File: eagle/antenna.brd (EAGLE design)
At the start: 127 x 76.2 mm, 21 parts

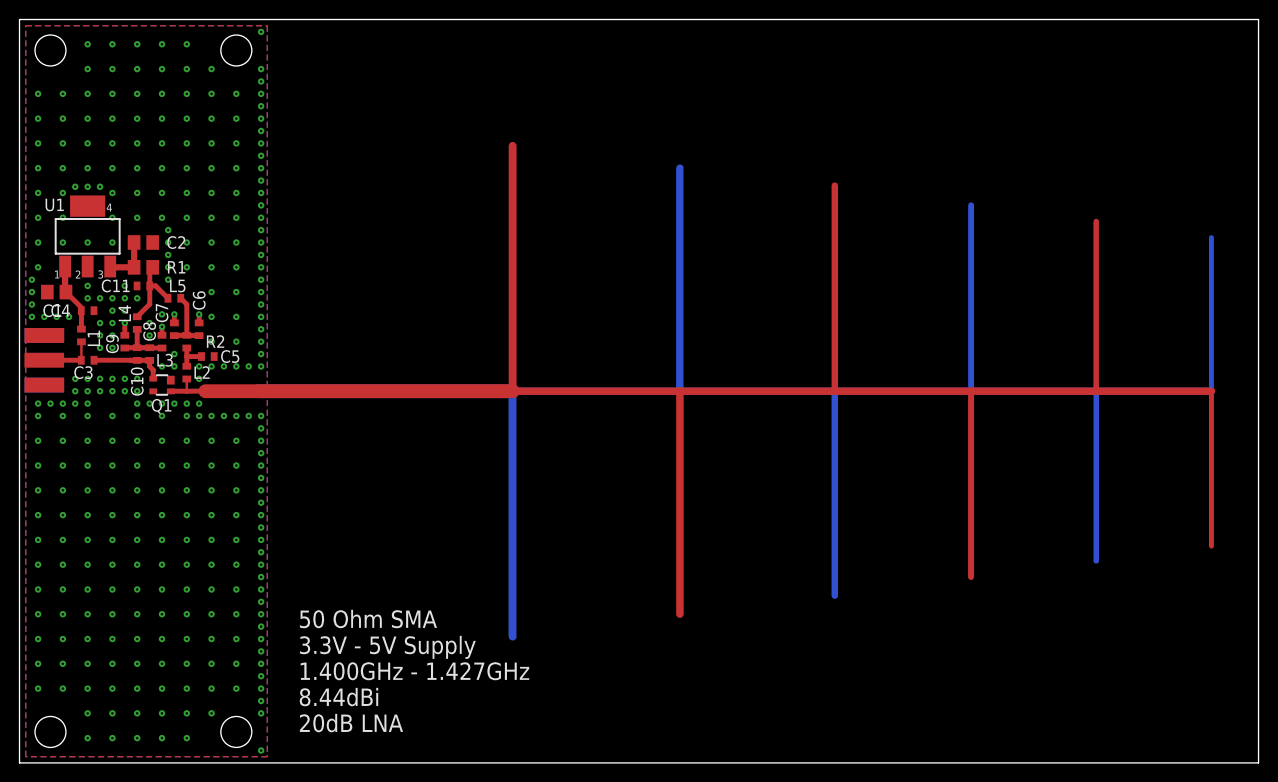
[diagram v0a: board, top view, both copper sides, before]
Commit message: cleaner antenna layout
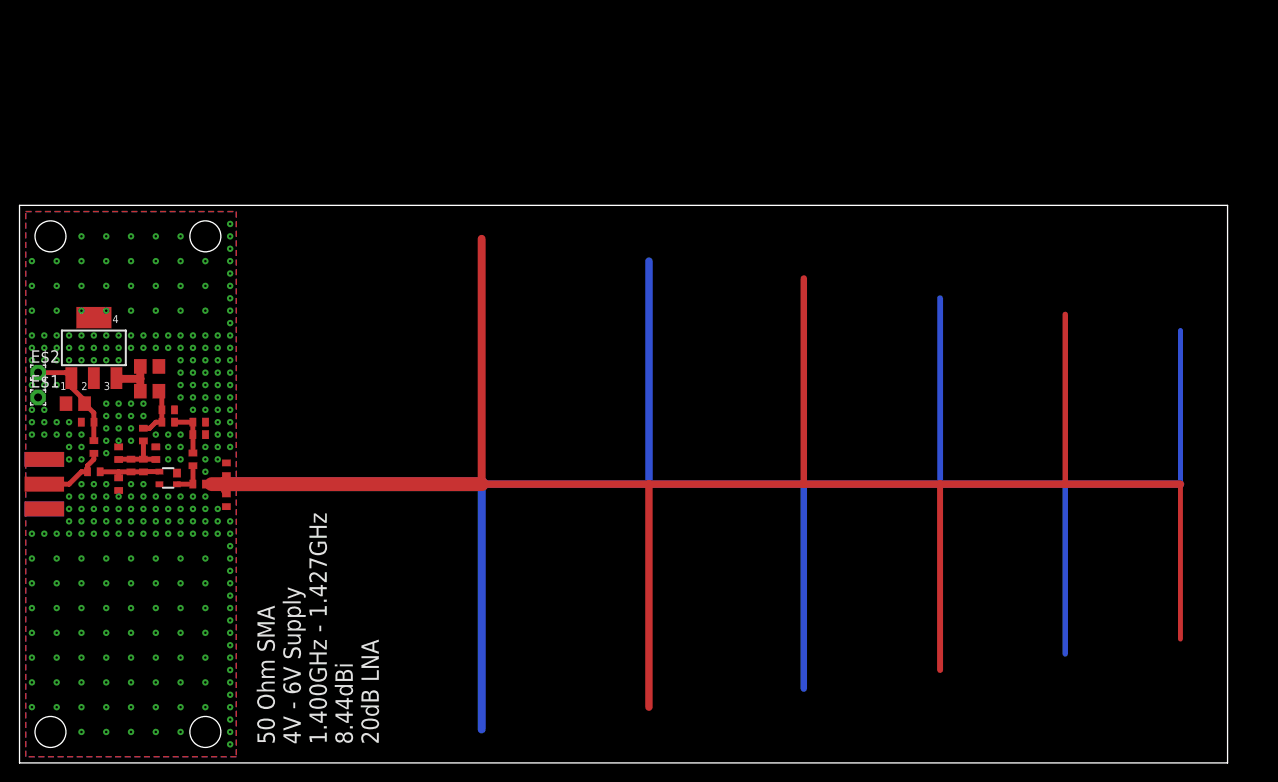
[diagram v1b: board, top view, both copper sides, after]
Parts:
- removed R2: (no value), ref-packages-longpad:R0402
- added C12, C13, C14: (no value), ref-packages-longpad:R0402
- added E$1, E$2: (no value), wirepad:1,6/0,8
- moved C5 16.0 mm to (10.2, 28.6), turned to 270 degrees
- moved C11 13.0 mm to (15.2, 36.2), turned to 0 degrees
- moved C2 12.7 mm to (13.3, 40.6)
- moved L5 12.7 mm to (15.2, 34.9)
- moved R1 12.7 mm to (13.3, 38.1)
- moved E$11 12.7 mm to (2.54, 26.0)
- moved C1 11.6 mm to (5.71, 36.8)
- moved L1 11.5 mm to (7.62, 32.4)
- moved C3 11.4 mm to (7.62, 29.8)
- moved C8 11.4 mm to (14.0, 31.8)
- moved C9 11.4 mm to (10.2, 31.8)
- moved L4 11.4 mm to (12.7, 33.7)
- moved U1 11.4 mm to (7.62, 42.5)
- moved C10 11.4 mm to (11.4, 30.5)
- moved L3 11.4 mm to (12.7, 30.5)
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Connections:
- net S$4 renamed VCC
- net S$5 renamed BIAS
- net S$6 renamed OUT
- removed net S$1: C6.1, C7.1, L5.1, R2.2
- removed net S$2: C5.1, L2.2, R2.1
- removed net S$3: C10.1, C3.1, L3.1, Q1.4
- new net AMP: C10.1, C3.1, C5.1, L3.1, Q1.4
- new net IN: C14.2, L2.1, Q1.2
- new net VBB: C6.1, C7.1, L2.2, L5.1
- net ANT: now also C12.2, C13.1, C14.1; no longer L2.1, Q1.2
- net GND: now also C12.1, C13.2, E$1.1
- net V5: now also E$2.1
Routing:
- net S$3: track 7.73 -> 0.00 mm
- net AMP: track 0.00 -> 6.69 mm
- net S$1: track 6.62 -> 0.00 mm
- net ANT: track 229.3 -> 223.4 mm
- net VBB: track 0.00 -> 5.04 mm
- net V5: track 6.78 -> 11.0 mm
- net GND: track 222.7 -> 218.8 mm, vias 323 -> 293
- net IN: track 0.00 -> 3.54 mm
- net S$2: track 3.38 -> 0.00 mm
- net BIAS: track 8.13 -> 5.45 mm
- net OUT: track 5.69 -> 7.14 mm
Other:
- board size 127 x 76.2 mm -> 123.8 x 57.1 mm
- board text added: "50 Ohm SMA 4V - 6V Supply 1.400GHz - 1.427GHz 8.44dBi 20dB LNA"
- board text removed: "50 Ohm SMA 3.3V - 5V Supply 1.400GHz - 1.427GHz 8.44dBi 20dB LNA"

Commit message: cleaner antenna layout
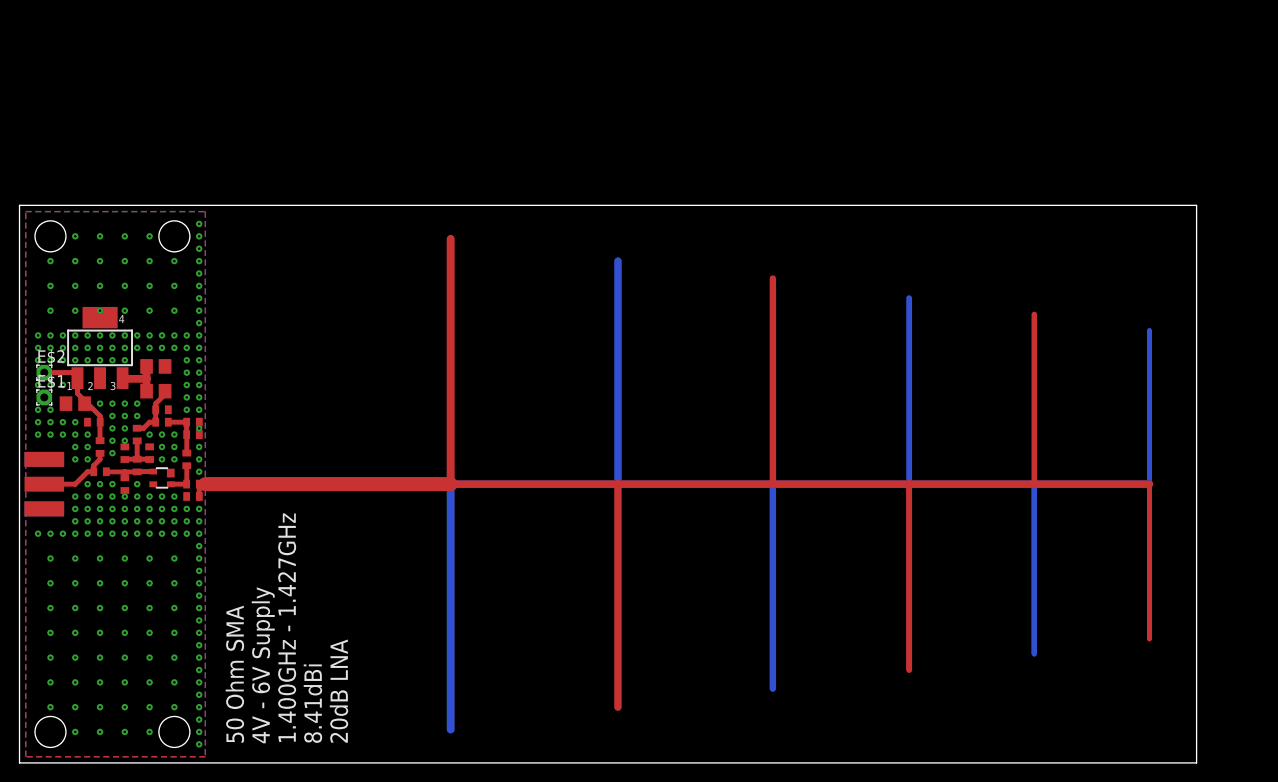
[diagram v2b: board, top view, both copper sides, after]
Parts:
- removed C10, C12, C13: (no value), ref-packages-longpad:R0402
- added C15: 68, ref-packages-longpad:R0402
- C1, C2: value (none) -> 1u
- C11, C4, C7, C8: value (none) -> 10n
- C14, C3, C6, C9: value (none) -> 1n
- L1, L2, L4: value (none) -> 22n
- L5: value (none) -> 51k
- R1: value (none) -> 220
- moved L2 0.64 mm to (17.1, 31.1)
- moved C3 0.64 mm to (8.26, 29.8)
- moved L1 0.64 mm to (8.26, 32.4)
- moved U1 0.64 mm to (8.26, 42.5)
- moved E$1 0.64 mm to (2.54, 37.5)
- moved E$2 0.64 mm to (2.54, 40.0)
- moved C11 0.63 mm to (14.6, 36.2)
- moved C2 0.63 mm to (14.0, 40.6)
- moved C4 0.63 mm to (7.62, 34.9)
- moved C5 0.63 mm to (10.8, 28.6)
- moved C8 0.63 mm to (13.3, 31.8)
- moved C9 0.63 mm to (10.8, 31.8)
- moved L3 0.63 mm to (12.1, 30.5)
- moved L4 0.63 mm to (12.1, 33.7)
- moved L5 0.63 mm to (14.6, 34.9)
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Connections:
- net AMP: no longer C10.1
- net ANT: now also C15.1; no longer C12.2, C13.1
- net GND: now also C15.2; no longer C12.1, C13.2
- net VCC: no longer C10.2
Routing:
- net ANT: track 223.4 -> 220.1 mm
- net VCC: track 5.75 -> 4.44 mm
- net AMP: track 6.69 -> 5.42 mm
- net GND: track 218.8 -> 217.9 mm, vias 293 -> 230
- net OUT: track 7.14 -> 7.75 mm
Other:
- board size 123.8 x 57.1 mm -> 120.7 x 57.1 mm
- board text added: "50 Ohm SMA 4V - 6V Supply 1.400GHz - 1.427GHz 8.41dBi 20dB LNA"
- board text removed: "50 Ohm SMA 4V - 6V Supply 1.400GHz - 1.427GHz 8.44dBi 20dB LNA"
